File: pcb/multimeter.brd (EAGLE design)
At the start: 99.1 x 68.6 mm, 66 parts, among them IC1 AD822R, IC2 MEGA32-A, IC3 25C080SN, Q1 BSS123, Q2 BSS123, Q3 BSS123, Q4 BSS123

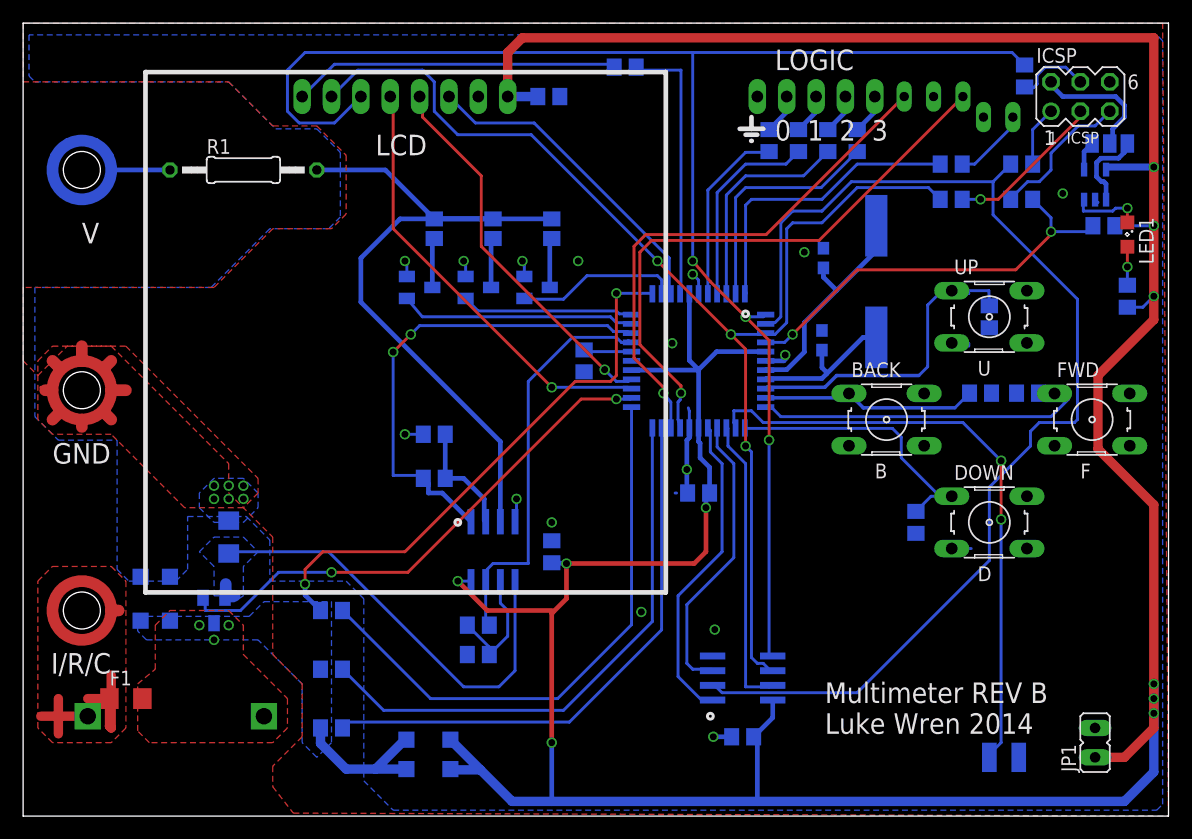
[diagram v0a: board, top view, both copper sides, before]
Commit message: added pcb files, connected charge LED to DC input instead of battery, connected Flash VCC to same net as IRD VCC
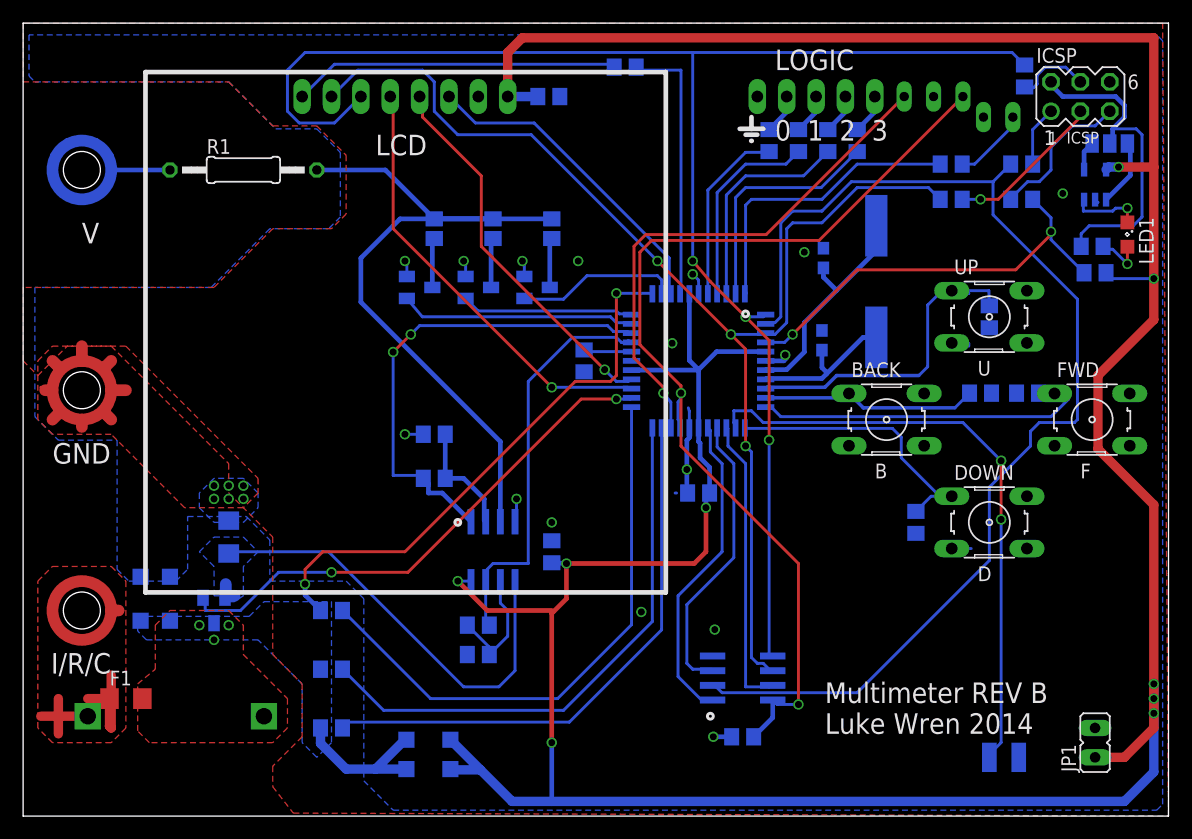
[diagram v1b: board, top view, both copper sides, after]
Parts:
- moved R20 5.29 mm to (92.5, 49.3), turned to 180 degrees
- moved R14 4.13 mm to (92.7, 47.0)
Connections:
- removed net IRD_VCC: IC2.19, U$3.E
- removed net N$19: ICSP.2, SJ1.2
- new net AUX_VCC: C3.1, IC2.19, IC3.8, U$3.E
- new net DC_IN: ICSP.2, R20.1, SJ1.2
- net VCC: no longer C3.1, IC3.8, R20.1
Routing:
- net AUX_VCC: track 0.00 -> 87.7 mm, vias 0 -> 2
- net IRD_VCC: track 50.3 -> 0.00 mm, vias 1 -> 0
- net DC_IN: track 0.00 -> 29.6 mm
- net VCC: track 308.1 -> 297.0 mm, vias 10 -> 9
- net N$19: track 11.1 -> 0.00 mm
- net N$22: track 7.31 -> 5.83 mm
- net N$21: track 36.1 -> 37.0 mm
- net N$23: track 3.33 -> 4.22 mm
